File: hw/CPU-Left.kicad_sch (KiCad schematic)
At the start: 32 parts, among them J3001 Conn_01x08, J3002 Conn_01x03, J3003 Conn_01x02, J3004 Conn_01x02, J3005 Conn_01x02, J3006 Conn_01x02, U3000 STM32F401XX-LQFP64, U3001 TLV62150A, Y3000 MCSJK-7I-8.00-18-30-60-B-30

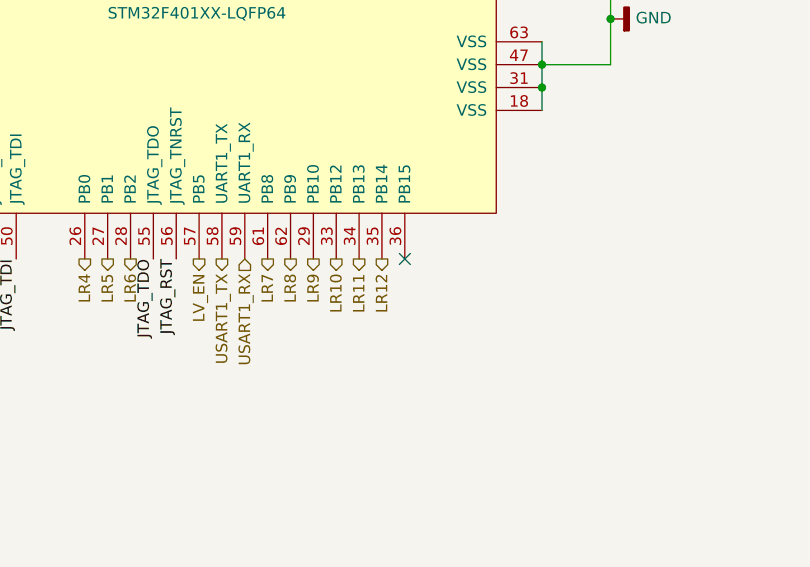
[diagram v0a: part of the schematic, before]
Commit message: Update schematic:
- Add ESD protection.
- Adjust distance bolts so they fit to the MX mounting plate.
- Make key layout symmetric.
- Add resistor to TX driver outputs.
- Use alternate IO functions on inter-board connectors.
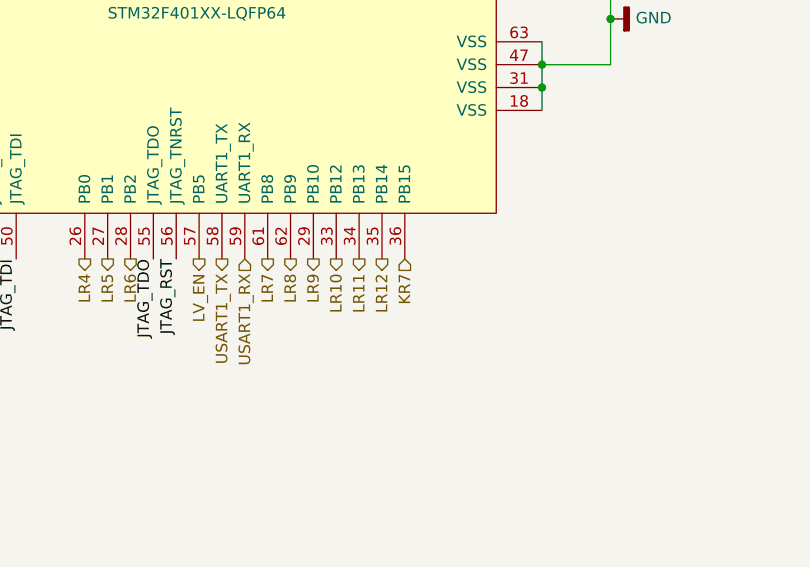
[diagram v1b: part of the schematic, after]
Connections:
- net KR7: now reaches U3000.36 (PB15)
- no-connect marks 5 -> 4
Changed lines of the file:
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@@
   )
   (no_connect (at 148.59 45.72))
-  (no_connect (at 184.15 106.68))
   (no_connect (at 83.82 91.44))
   (no_connect (at 140.97 45.72))
@@
     (effects (font (size 1.27 1.27)) (justify right))
   )
+  (hierarchical_label "KR7" (shape input) (at 184.15 106.68 270)
+    (effects (font (size 1.27 1.27)) (justify right))
+  )

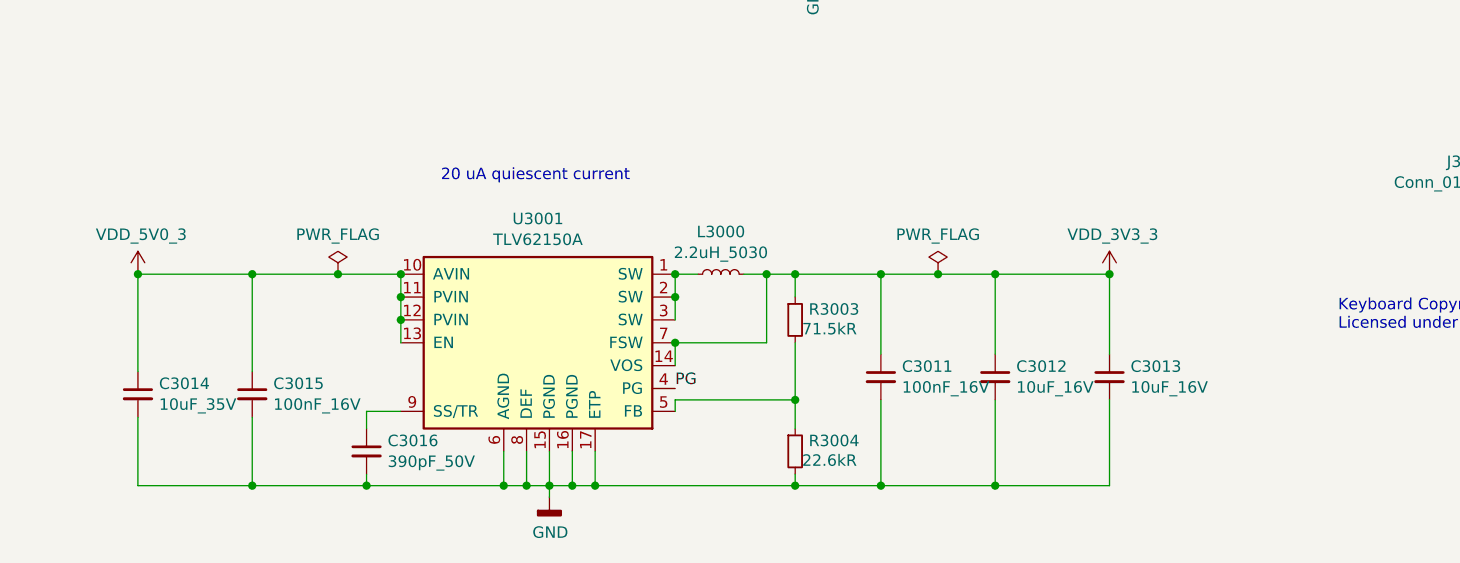
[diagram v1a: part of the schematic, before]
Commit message: Add current probes to 3.3V and pull-up to LV_EN.
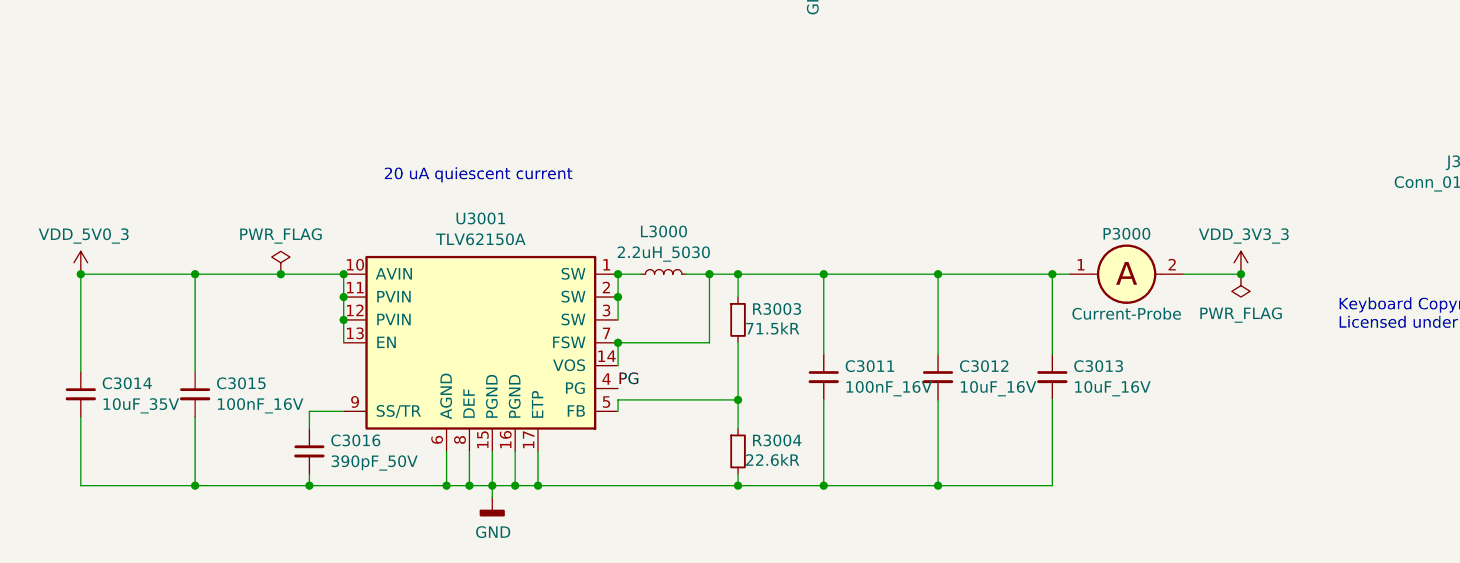
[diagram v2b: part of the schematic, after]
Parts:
- added P3000: Current-Probe, Keyboard:Current-Probe-2.54, symbol Keyboard:Current-Probe
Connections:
- net VDD_3V3_3: now also P3000.2; no longer C3011.1, C3012.1, C3013.1, L3000.2, R3003.1, U3001.14 (VOS), U3001.7 (FSW)
- new net: C3011.1, C3012.1, C3013.1, L3000.2, P3000.1, R3003.1, U3001.14 (VOS), U3001.7 (FSW)
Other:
- moved on the sheet: C3011, C3012, C3013, C3014, C3015, C3016, L3000, R3003, R3004, U3001
